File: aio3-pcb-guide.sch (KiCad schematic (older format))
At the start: 1 part

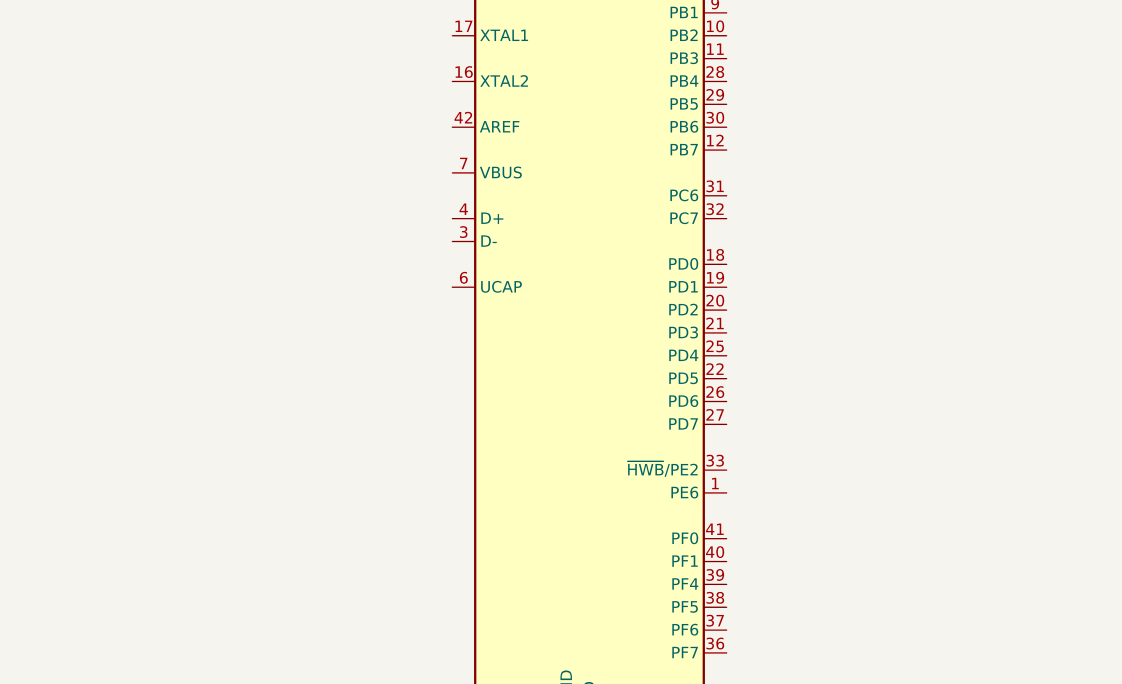
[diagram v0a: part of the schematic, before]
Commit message: [schema](mcu): add pull-down and usb resistors
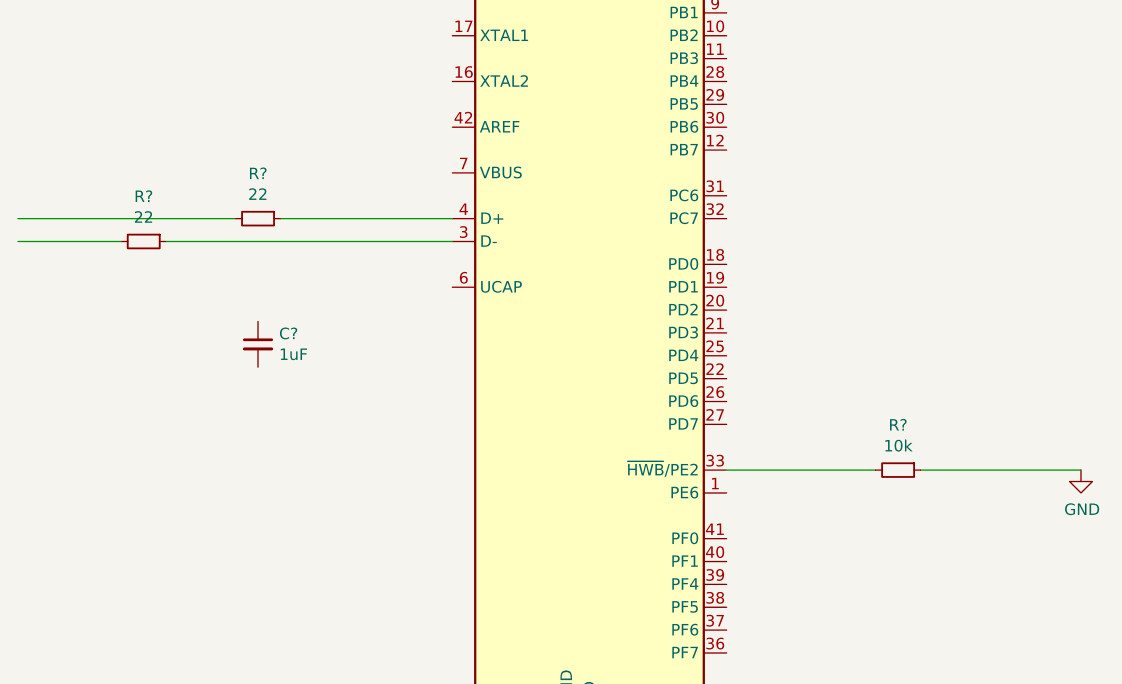
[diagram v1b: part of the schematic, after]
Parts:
- added C?: 1uF, symbol Device:C_Small
- added R?: 10k, symbol Device:R_Small
- added R? (x2): 22, symbol Device:R_Small
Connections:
- wire segments 6 -> 12
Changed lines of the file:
@@
 	3200 5150 3100 5150
 Connection ~ 3100 5150
+$Comp
+L Device:R_Small R?
+U 1 1 61F7F9BB
+P 4550 3950
+F 0 "R?" V 4354 3950 50  0000 C CNN
+F 1 "10k" V 4445 3950 50  0000 C CNN
+F 2 "" H 4550 3950 50  0001 C CNN
+F 3 "~" H 4550 3950 50  0001 C CNN
+	1    4550 3950
+	0    1    1    0
+$EndComp
+Wire Wire Line
+	3800 3950 4450 3950
+$Comp
+L power:GND #PWR?
+U 1 1 61F83000
+P 5350 3950
+F 0 "#PWR?" H 5350 3700 50  0001 C CNN
+F 1 "GND" H 5355 3777 50  0000 C CNN
+F 2 "" H 5350 3950 50  0001 C CNN
+F 3 "" H 5350 3950 50  0001 C CNN
+	1    5350 3950
+	1    0    0    -1
+$EndComp
+Wire Wire Line
+	5350 3950 4650 3950
+$Comp
+L Device:R_Small R?
+U 1 1 61F83B8A
+P 1750 2850
+F 0 "R?" V 1554 2850 50  0000 C CNN
+F 1 "22" V 1645 2850 50  0000 C CNN
+F 2 "" H 1750 2850 50  0001 C CNN
+F 3 "~" H 1750 2850 50  0001 C CNN
+	1    1750 2850
+	0    1    1    0
+$EndComp
+$Comp
+L Device:R_Small R?
+U 1 1 61F845FD
+P 1250 2950
+F 0 "R?" V 1054 2950 50  0000 C CNN
+F 1 "22" V 1145 2950 50  0000 C CNN
+F 2 "" H 1250 2950 50  0001 C CNN
+F 3 "~" H 1250 2950 50  0001 C CNN
+	1    1250 2950
+	0    1    1    0
+$EndComp
+Wire Wire Line
+	2600 2850 1850 2850
+Wire Wire Line
+	1350 2950 2600 2950
+Wire Wire Line
+	1150 2950 700  2950
+Wire Wire Line
+	1650 2850 700  2850
+$Comp
+L Device:C_Small C?
+U 1 1 61F85CD3
+P 1750 3400
+F 0 "C?" H 1842 3446 50  0000 L CNN
+F 1 "1uF" H 1842 3355 50  0000 L CNN
+F 2 "" H 1750 3400 50  0001 C CNN
+F 3 "~" H 1750 3400 50  0001 C CNN
+	1    1750 3400
+	1    0    0    -1
+$EndComp
 $EndSCHEMATC

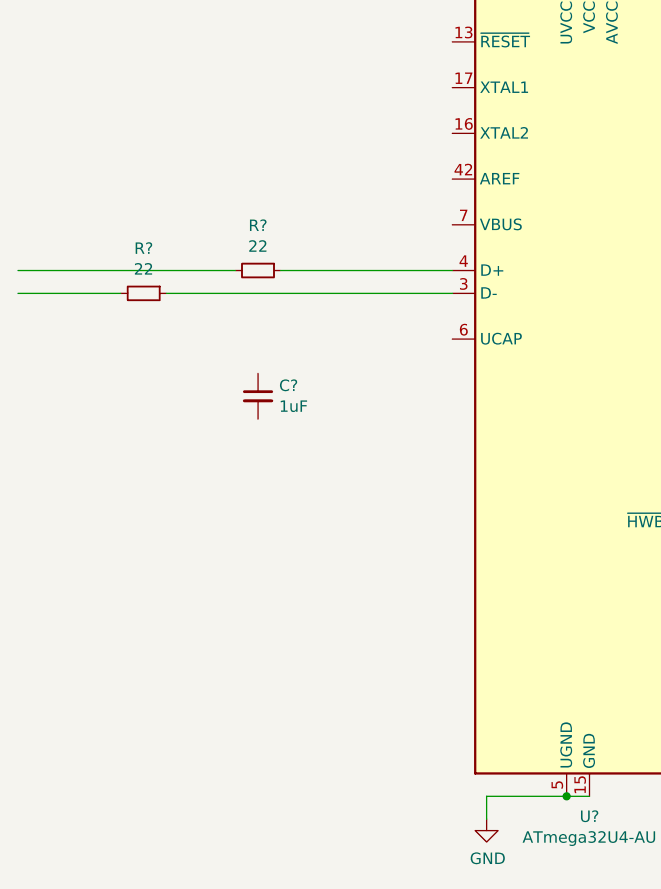
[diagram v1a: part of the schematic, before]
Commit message: [schema](mcu): add decoupling capacitors
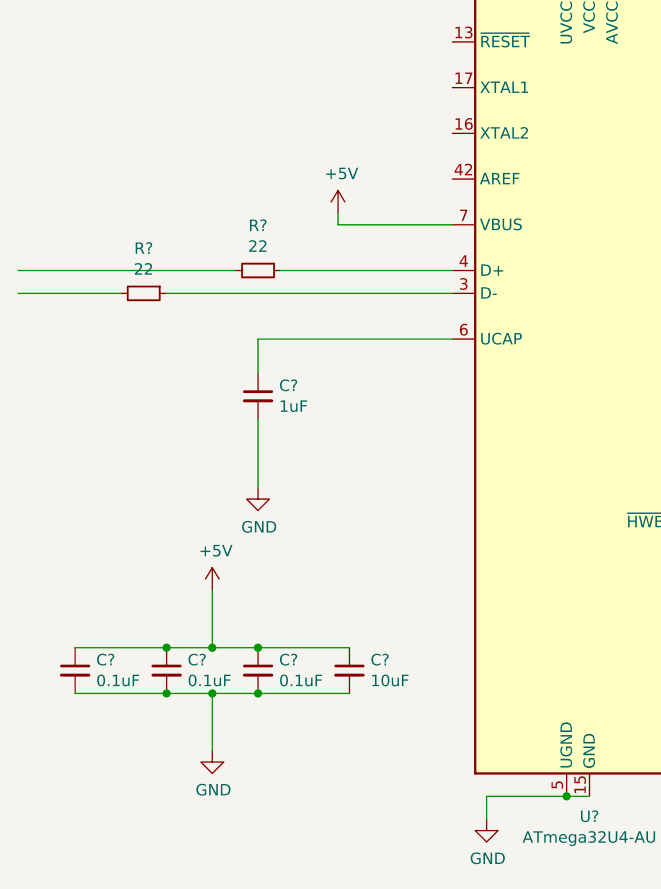
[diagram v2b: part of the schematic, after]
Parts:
- added C? (x3): 0.1uF, symbol Device:C_Small
- added C?: 10uF, symbol Device:C_Small
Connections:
- wire segments 12 -> 27
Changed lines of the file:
@@
 	1    0    0    -1
 $EndComp
+Wire Wire Line
+	2600 3150 1750 3150
+Wire Wire Line
+	1750 3150 1750 3300
+$Comp
+L power:GND #PWR?
+U 1 1 61F888E9
+P 1750 3800
+F 0 "#PWR?" H 1750 3550 50  0001 C CNN
+F 1 "GND" H 1755 3627 50  0000 C CNN
+F 2 "" H 1750 3800 50  0001 C CNN
+F 3 "" H 1750 3800 50  0001 C CNN
+	1    1750 3800
+	1    0    0    -1
+$EndComp
+Wire Wire Line
+	1750 3500 1750 3800
+$Comp
+L Device:C_Small C?
+U 1 1 61F892A7
+P 950 4600
+F 0 "C?" H 1042 4646 50  0000 L CNN
+F 1 "0.1uF" H 1042 4555 50  0000 L CNN
+F 2 "" H 950 4600 50  0001 C CNN
+F 3 "~" H 950 4600 50  0001 C CNN
+	1    950  4600
+	1    0    0    -1
+$EndComp
+$Comp
+L Device:C_Small C?
+U 1 1 61F8942D
+P 1350 4600
+F 0 "C?" H 1442 4646 50  0000 L CNN
+F 1 "0.1uF" H 1442 4555 50  0000 L CNN
+F 2 "" H 1350 4600 50  0001 C CNN
+F 3 "~" H 1350 4600 50  0001 C CNN
+	1    1350 4600
+	1    0    0    -1
+$EndComp
+$Comp
+L Device:C_Small C?
+U 1 1 61F8998B
+P 1750 4600
+F 0 "C?" H 1842 4646 50  0000 L CNN
+F 1 "0.1uF" H 1842 4555 50  0000 L CNN
+F 2 "" H 1750 4600 50  0001 C CNN
+F 3 "~" H 1750 4600 50  0001 C CNN
+	1    1750 4600
+	1    0    0    -1
+$EndComp
+$Comp
+L Device:C_Small C?
+U 1 1 61F89E9F
+P 2150 4600
+F 0 "C?" H 2242 4646 50  0000 L CNN
+F 1 "10uF" H 2242 4555 50  0000 L CNN
+F 2 "" H 2150 4600 50  0001 C CNN
+F 3 "~" H 2150 4600 50  0001 C CNN
+	1    2150 4600
+	1    0    0    -1
+$EndComp
+Wire Wire Line
+	950  4500 1350 4500
+Wire Wire Line
+	1350 4500 1550 4500
+Connection ~ 1350 4500
+Wire Wire Line
+	1750 4500 2150 4500
+Connection ~ 1750 4500
+Wire Wire Line
+	2150 4700 1750 4700
+Wire Wire Line
+	1350 4700 950  4700
+Wire Wire Line
+	1350 4700 1550 4700
+Connection ~ 1350 4700
+Connection ~ 1750 4700
+$Comp
+L power:GND #PWR?
+U 1 1 61F8C302
+P 1550 4950
+F 0 "#PWR?" H 1550 4700 50  0001 C CNN
+F 1 "GND" H 1555 4777 50  0000 C CNN
+F 2 "" H 1550 4950 50  0001 C CNN
+F 3 "" H 1550 4950 50  0001 C CNN
+	1    1550 4950
+	1    0    0    -1
+$EndComp
+Wire Wire Line
+	1550 4700 1550 4950
+Connection ~ 1550 4700
+Wire Wire Line
+	1550 4700 1750 4700
+$Comp
+L power:+5V #PWR?
+U 1 1 61F8CCFB
+P 1550 4250
+F 0 "#PWR?" H 1550 4100 50  0001 C CNN
+F 1 "+5V" H 1565 4423 50  0000 C CNN
+F 2 "" H 1550 4250 50  0001 C CNN
+F 3 "" H 1550 4250 50  0001 C CNN
+	1    1550 4250
+	1    0    0    -1
+$EndComp
+Wire Wire Line
+	1550 4250 1550 4500
+Connection ~ 1550 4500
+Wire Wire Line
+	1550 4500 1750 4500
+$Comp
+L power:+5V #PWR?
+U 1 1 61F8D879
+P 2100 2600
+F 0 "#PWR?" H 2100 2450 50  0001 C CNN
+F 1 "+5V" H 2115 2773 50  0000 C CNN
+F 2 "" H 2100 2600 50  0001 C CNN
+F 3 "" H 2100 2600 50  0001 C CNN
+	1    2100 2600
+	1    0    0    -1
+$EndComp
+Wire Wire Line
+	2100 2600 2100 2650
+Wire Wire Line
+	2100 2650 2600 2650
 $EndSCHEMATC

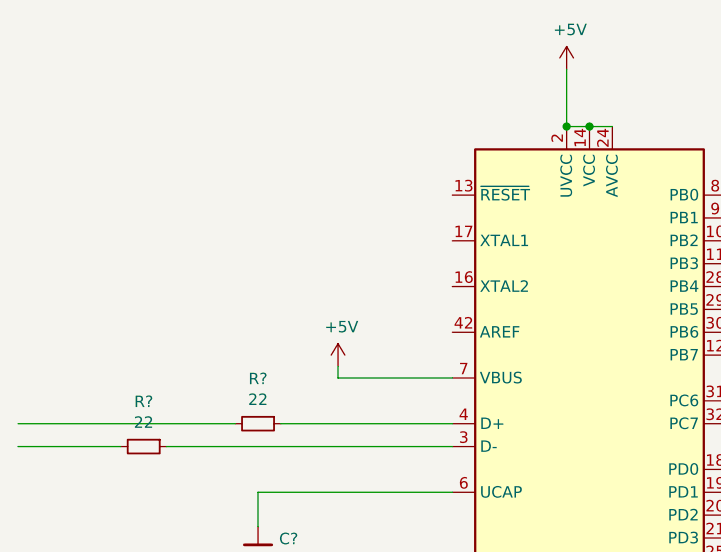
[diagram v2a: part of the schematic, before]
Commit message: [schema](mcu): add crystal
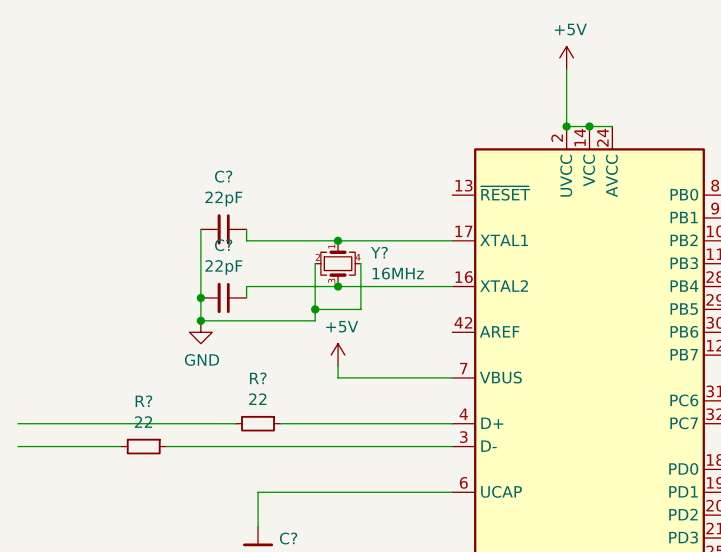
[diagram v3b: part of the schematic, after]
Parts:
- added C? (x2): 22pF, symbol Device:C_Small
- added Y?: 16MHz, symbol Device:Crystal_GND24_Small
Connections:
- wire segments 27 -> 40
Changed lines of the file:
@@
 Wire Wire Line
 	2100 2650 2600 2650
+$Comp
+L Device:Crystal_GND24_Small Y?
+U 1 1 61F8EF88
+P 2100 2150
+F 0 "Y?" V 2054 2294 50  0000 L CNN
+F 1 "16MHz" V 2145 2294 50  0000 L CNN
+F 2 "" H 2100 2150 50  0001 C CNN
+F 3 "~" H 2100 2150 50  0001 C CNN
+	1    2100 2150
+	0    1    1    0
+$EndComp
+$Comp
+L power:GND #PWR?
+U 1 1 61F93FA6
+P 1500 2400
+F 0 "#PWR?" H 1500 2150 50  0001 C CNN
+F 1 "GND" H 1505 2227 50  0000 C CNN
+F 2 "" H 1500 2400 50  0001 C CNN
+F 3 "" H 1500 2400 50  0001 C CNN
+	1    1500 2400
+	1    0    0    -1
+$EndComp
+Wire Wire Line
+	2100 2050 2600 2050
+Wire Wire Line
+	2100 2250 2600 2250
+$Comp
+L Device:C_Small C?
+U 1 1 61F98037
+P 1600 2000
+F 0 "C?" V 1371 2000 50  0000 C CNN
+F 1 "22pF" V 1462 2000 50  0000 C CNN
+F 2 "" H 1600 2000 50  0001 C CNN
+F 3 "~" H 1600 2000 50  0001 C CNN
+	1    1600 2000
+	0    1    1    0
+$EndComp
+$Comp
+L Device:C_Small C?
+U 1 1 61F99075
+P 1600 2300
+F 0 "C?" V 1371 2300 50  0000 C CNN
+F 1 "22pF" V 1462 2300 50  0000 C CNN
+F 2 "" H 1600 2300 50  0001 C CNN
+F 3 "~" H 1600 2300 50  0001 C CNN
+	1    1600 2300
+	0    1    1    0
+$EndComp
+Wire Wire Line
+	1500 2000 1500 2300
+Wire Wire Line
+	1500 2300 1500 2400
+Connection ~ 1500 2300
+Wire Wire Line
+	2100 2050 1700 2050
+Wire Wire Line
+	1700 2050 1700 2000
+Connection ~ 2100 2050
+Wire Wire Line
+	2100 2250 1700 2250
+Wire Wire Line
+	1700 2250 1700 2300
+Connection ~ 2100 2250
+Wire Wire Line
+	2000 2150 2000 2350
+Wire Wire Line
+	2000 2400 1500 2400
+Connection ~ 1500 2400
+Wire Wire Line
+	2200 2150 2200 2350
+Wire Wire Line
+	2200 2350 2000 2350
+Connection ~ 2000 2350
+Wire Wire Line
+	2000 2350 2000 2400
 $EndSCHEMATC

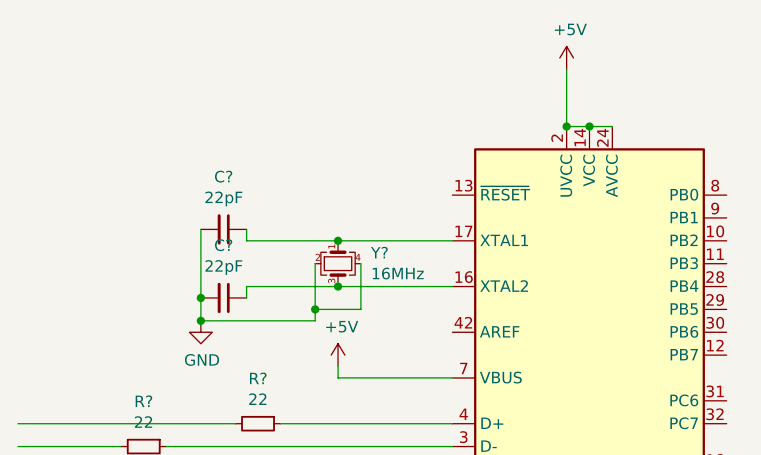
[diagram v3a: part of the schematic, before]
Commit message: [schema](mcu): add reset switch
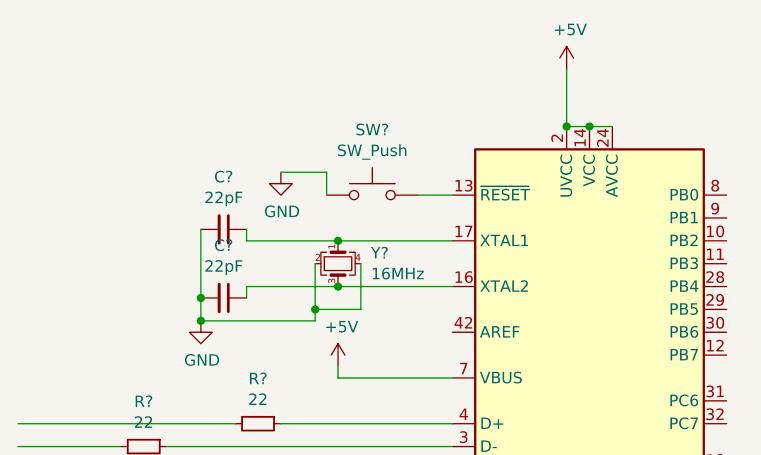
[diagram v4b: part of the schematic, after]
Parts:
- added SW?: SW_Push, symbol Switch:SW_Push
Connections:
- wire segments 40 -> 43
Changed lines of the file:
@@
 Wire Wire Line
 	2000 2350 2000 2400
+$Comp
+L Switch:SW_Push SW?
+U 1 1 61F9CBA8
+P 2250 1850
+F 0 "SW?" H 2250 2135 50  0000 C CNN
+F 1 "SW_Push" H 2250 2044 50  0000 C CNN
+F 2 "" H 2250 2050 50  0001 C CNN
+F 3 "~" H 2250 2050 50  0001 C CNN
+	1    2250 1850
+	1    0    0    -1
+$EndComp
+$Comp
+L power:GND #PWR?
+U 1 1 61F9DFD1
+P 1850 1750
+F 0 "#PWR?" H 1850 1500 50  0001 C CNN
+F 1 "GND" H 1855 1577 50  0000 C CNN
+F 2 "" H 1850 1750 50  0001 C CNN
+F 3 "" H 1850 1750 50  0001 C CNN
+	1    1850 1750
+	1    0    0    -1
+$EndComp
+Wire Wire Line
+	2050 1850 2050 1750
+Wire Wire Line
+	2050 1750 1850 1750
+Wire Wire Line
+	2450 1850 2600 1850
 $EndSCHEMATC

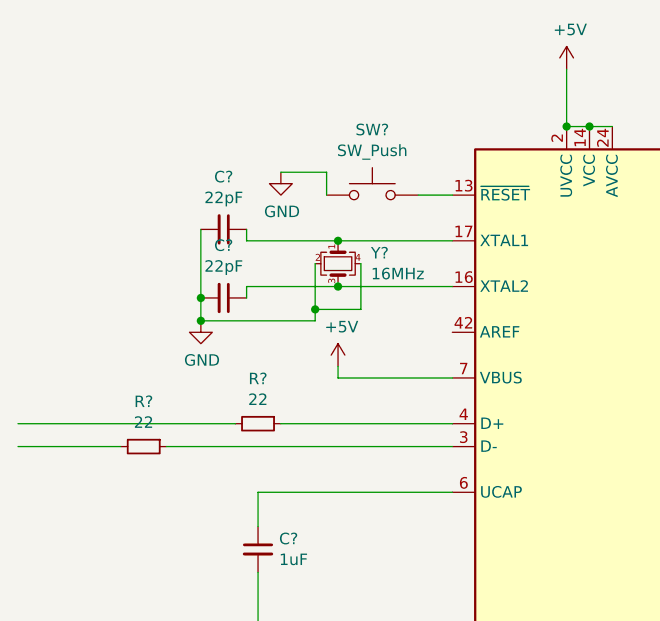
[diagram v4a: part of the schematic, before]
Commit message: [schema](mcu): add global nets
 - end of part 3
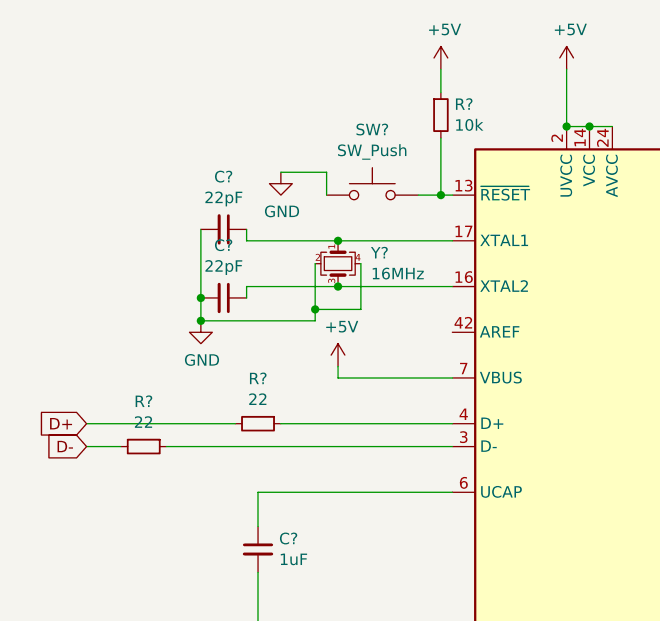
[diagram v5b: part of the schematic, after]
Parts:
- added R?: 10k, symbol Device:R_Small
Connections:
- net labels added: D+, D-
- wire segments 43 -> 46
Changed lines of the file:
@@
 $EndComp
-Wire Wire Line
-	2600 2850 1850 2850
 Wire Wire Line
 	1350 2950 2600 2950
-Wire Wire Line
-	1150 2950 700  2950
-Wire Wire Line
-	1650 2850 700  2850
 $Comp
 L Device:C_Small C?
@@
 	2050 1750 1850 1750
 Wire Wire Line
-	2450 1850 2600 1850
+	2450 1850 2550 1850
+$Comp
+L Device:R_Small R?
+U 1 1 61FA0370
+P 2550 1500
+F 0 "R?" H 2609 1546 50  0000 L CNN
+F 1 "10k" H 2609 1455 50  0000 L CNN
+F 2 "" H 2550 1500 50  0001 C CNN
+F 3 "~" H 2550 1500 50  0001 C CNN
+	1    2550 1500
+	1    0    0    -1
+$EndComp
+Wire Wire Line
+	2550 1850 2550 1600
+Connection ~ 2550 1850
+Wire Wire Line
+	2550 1850 2600 1850
+$Comp
+L power:+5V #PWR?
+U 1 1 61FA1EE4
+P 2550 1300
+F 0 "#PWR?" H 2550 1150 50  0001 C CNN
+F 1 "+5V" H 2565 1473 50  0000 C CNN
+F 2 "" H 2550 1300 50  0001 C CNN
+F 3 "" H 2550 1300 50  0001 C CNN
+	1    2550 1300
+	1    0    0    -1
+$EndComp
+Wire Wire Line
+	2550 1400 2550 1300
+Wire Wire Line
+	2600 2850 1850 2850
+Text GLabel 1000 2850 0    50   Input ~ 0
+D+
+Text GLabel 1000 2950 0    50   Input ~ 0
+D-
+Wire Wire Line
+	1000 2950 1150 2950
+Wire Wire Line
+	1650 2850 1000 2850
 $EndSCHEMATC

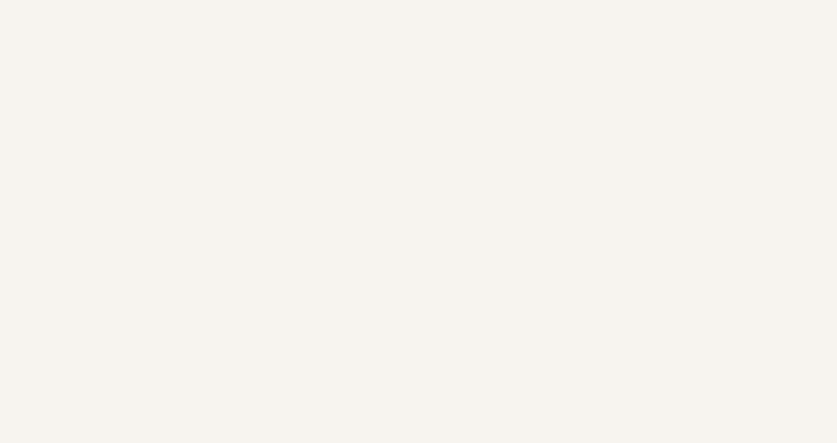
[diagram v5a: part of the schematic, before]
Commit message: [schema](usb): add usb circuitry
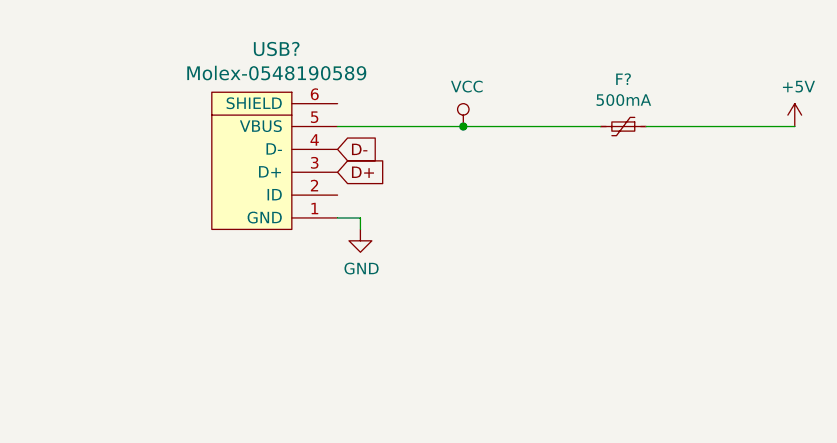
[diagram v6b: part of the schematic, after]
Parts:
- added F?: 500mA, symbol Device:Polyfuse_Small
- added USB?: Molex-0548190589, symbol random-keyboard-parts:Molex-0548190589
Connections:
- net +5V: now also F?.1
- net D+: now also USB?.3 (D+)
- net D-: now also USB?.4 (D-)
- net GND: now also USB?.1 (GND)
- new net VCC: F?.2, USB?.5 (VBUS)
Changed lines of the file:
@@
 EESchema Schematic File Version 4
+LIBS:aio3-pcb-guide-cache
 EELAYER 30 0
 EELAYER END
@@
 Wire Wire Line
 	1650 2850 1000 2850
+$Comp
+L Device:Polyfuse_Small F?
+U 1 1 61FA55FC
+P 7350 1550
+F 0 "F?" V 7145 1550 50  0000 C CNN
+F 1 "500mA" V 7236 1550 50  0000 C CNN
+F 2 "" H 7400 1350 50  0001 L CNN
+F 3 "~" H 7350 1550 50  0001 C CNN
+	1    7350 1550
+	0    1    1    0
+$EndComp
+$Comp
+L random-keyboard-parts:Molex-0548190589 USB?
+U 1 1 61FA7777
+P 5800 1750
+F 0 "USB?" V 6337 1717 60  0000 C CNN
+F 1 "Molex-0548190589" V 6231 1717 60  0000 C CNN
+F 2 "" H 5800 1750 60  0001 C CNN
+F 3 "" H 5800 1750 60  0001 C CNN
+	1    5800 1750
+	0    -1   -1   0
+$EndComp
+$Comp
+L power:+5V #PWR?
+U 1 1 61FB5CF4
+P 8100 1550
+F 0 "#PWR?" H 8100 1400 50  0001 C CNN
+F 1 "+5V" H 8115 1723 50  0000 C CNN
+F 2 "" H 8100 1550 50  0001 C CNN
+F 3 "" H 8100 1550 50  0001 C CNN
+	1    8100 1550
+	1    0    0    -1
+$EndComp
+Wire Wire Line
+	8100 1550 7450 1550
+Wire Wire Line
+	6100 1550 6650 1550
+$Comp
+L power:VCC #PWR?
+U 1 1 61FB7392
+P 6650 1550
+F 0 "#PWR?" H 6650 1400 50  0001 C CNN
+F 1 "VCC" H 6667 1723 50  0000 C CNN
+F 2 "" H 6650 1550 50  0001 C CNN
+F 3 "" H 6650 1550 50  0001 C CNN
+	1    6650 1550
+	1    0    0    -1
+$EndComp
+Connection ~ 6650 1550
+Wire Wire Line
+	6650 1550 7250 1550
+Text GLabel 6100 1750 2    50   Input ~ 0
+D+
+Text GLabel 6100 1650 2    50   Input ~ 0
+D-
+$Comp
+L power:GND #PWR?
+U 1 1 61FBA386
+P 6200 2000
+F 0 "#PWR?" H 6200 1750 50  0001 C CNN
+F 1 "GND" H 6205 1827 50  0000 C CNN
+F 2 "" H 6200 2000 50  0001 C CNN
+F 3 "" H 6200 2000 50  0001 C CNN
+	1    6200 2000
+	1    0    0    -1
+$EndComp
+Wire Wire Line
+	6200 2000 6200 1950
+Wire Wire Line
+	6200 1950 6100 1950
 $EndSCHEMATC
